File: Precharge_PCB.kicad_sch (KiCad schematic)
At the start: 73 parts, among them J1 Conn_01x02, J10 Conn_01x06, J2 Conn_01x02, J3 Conn_01x08, J4 Conn_01x02, J5 Conn_01x03, J9 Conn_01x02, K1 G2RL-1A, K2 G2RL-1A, Q1 DMN61D8LQ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

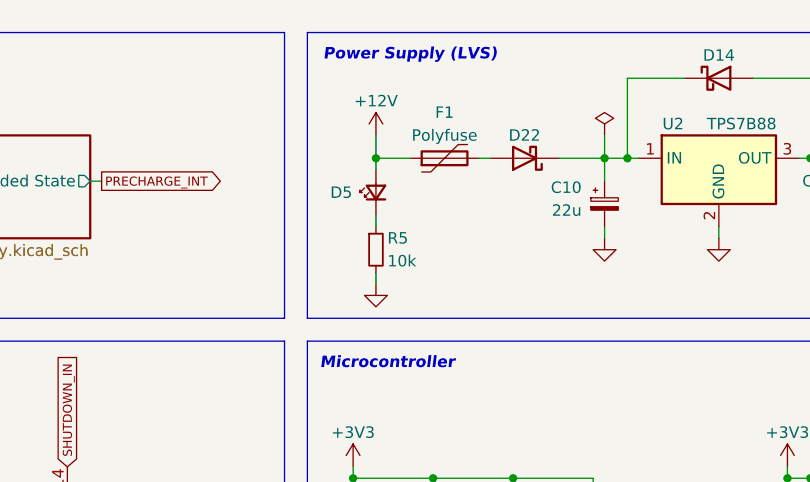
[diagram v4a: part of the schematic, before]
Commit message: schematic: Add a TVS diode to the LVS input
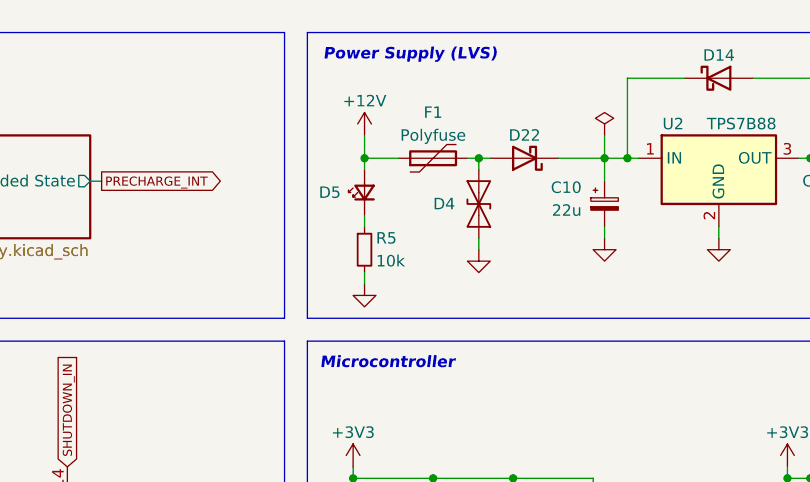
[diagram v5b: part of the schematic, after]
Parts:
- added D4: SMAJ24CA, Diode_SMD:D_SMA, symbol Diode:SMAJ24CA
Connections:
- net GND: now also D4.1 (A1)
- net at D22.2 (A), F1.2: now also D4.2 (A2)
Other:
- moved on the sheet: D5, F1, R5
